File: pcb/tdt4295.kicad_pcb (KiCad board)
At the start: 6 copper layers, 119.8 x 96.8 mm, 156 parts, among them J1 FPGA_DEBUG, J2 DE15_Socket_HighDensity, J4 Conn_ST_STDC14, J5 Micro_SD_Card, J6 Conn_02x05_Odd_Even, J7 USB_C_Receptacle_USB2.0_14P, J8 USB_C_Receptacle_USB2.0_14P, SW1 SW_BLUE, SW2 SW_BLACK, U1 XC7A50T-FTG256, U2 S70KL1283DPBHV020, U3 W25Q128JVS, U4 TPS54325PWP.d, U5 TPS54294PWP, U6 STM32U595ZJTx, U7 TPS2051CDBV, U8 USBLC6-2SC6, Y1 ASE-20MHz, Y2 16MHz

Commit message: fixed psd footprintgs and some routing
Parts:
- J6: footprint Connector_PinHeader_2.54mm:PinHeader_2x05_P2.54mm_Vertical_SMD -> Connector_PinHeader_2.54mm:PinHeader_2x05_P2.54mm_Vertical
- U5: footprint Package_SO:HTSSOP-16-1EP_4.4x5mm_P0.65mm_EP3.4x5mm_Mask2.46x2.31mm -> TPS54294PWP:PWP16_2P31X2P46
- moved J6 5.63 mm to (69.9, 135.3), turned to 90 degrees
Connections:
- J6 pad 1: /Powersupply/5V_IN -> 5V_IN
- J7 pad A4: /power_source/5V_IN -> 5V_IN
- J7 pad A9: /power_source/5V_IN -> 5V_IN
- J7 pad B4: /power_source/5V_IN -> 5V_IN
- J7 pad B9: /power_source/5V_IN -> 5V_IN
- R57 pad 1: /power_source/5V_IN -> 5V_IN
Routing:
- net 5V_IN: track 0.00 -> 29.1 mm, vias 0 -> 2
- net POWER_IN: track 105.4 -> 85.4 mm, vias 6 -> 4
- net USER_BUTTON: track 85.1 -> 76.2 mm
- net GND: track 454.5 -> 459.3 mm, vias 125 -> 123

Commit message: fixed many errors and violations
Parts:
- moved C25 0.24 mm to (123.2, 103.3)
- moved R46 0.11 mm to (134.7, 73.6)
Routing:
- net /Powersupply/1V0_OUT: track 0.00 -> 68.1 mm, vias 0 -> 4
- net /Powersupply/1V8_OUT: track 0.00 -> 48.7 mm, vias 0 -> 2
- net +1V8: track 70.1 -> 111.6 mm, vias 6 -> 11
- net +3V3: track 174.9 -> 213.3 mm, vias 66 -> 68
- net /Powersupply/3V3_OUT: track 11.1 -> 49.1 mm, vias 1 -> 3
- net +1V0: track 114.0 -> 144.5 mm, vias 8 -> 13
- net POWER_IN: track 85.4 -> 95.5 mm
- net GND: track 459.3 -> 469.2 mm, vias 123 -> 122
- net Net-(J8-D+-PadA6): track 7.98 -> 9.72 mm
- net Net-(U7-OUT): track 27.2 -> 28.8 mm
- net Net-(U1A-IO_L23N_T3_A02_D18_14): track 17.2 -> 17.8 mm, vias 1 -> 2

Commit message: fixed all unconnected errors
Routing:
- net +1V8: track 111.6 -> 136.5 mm
- net +1V0: track 144.5 -> 163.4 mm
- net GND: track 469.2 -> 475.9 mm

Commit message: labeled usb data +/- conn and diff-paired them
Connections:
- net Net-(J8-D+-PadA6) renamed /MCU/host_port/D+
- net Net-(J8-D--PadA7) renamed /MCU/host_port/D-
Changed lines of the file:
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@@
 			(layers "F.Cu" "F.Mask" "F.Paste")
 			(roundrect_rratio 0.25)
-			(net "Net-(J8-D+-PadA6)")
+			(net "/MCU/host_port/D+")
 			(pinfunction "I/O1_1")
 			(pintype "passive")
@@
 			(layers "F.Cu" "F.Mask" "F.Paste")
 			(roundrect_rratio 0.25)
-			(net "Net-(J8-D--PadA7)")
+			(net "/MCU/host_port/D-")
 			(pinfunction "I/O2_3")
 			(pintype "passive")
@@
 			(layers "F.Cu" "F.Mask" "F.Paste")
 			(roundrect_rratio 0.25)
-			(net "Net-(J8-D+-PadA6)")
+			(net "/MCU/host_port/D+")
 			(pinfunction "D+_A6")
 			(pintype "bidirectional")
@@
 			(layers "F.Cu" "F.Mask" "F.Paste")
 			(roundrect_rratio 0.25)
-			(net "Net-(J8-D--PadA7)")
+			(net "/MCU/host_port/D-")
 			(pinfunction "D-_A7")
 			(pintype "bidirectional")
@@
 			(layers "F.Cu" "F.Mask" "F.Paste")
 			(roundrect_rratio 0.25)
-			(net "Net-(J8-D+-PadA6)")
+			(net "/MCU/host_port/D+")
 			(pinfunction "D+_B6")
 			(pintype "bidirectional")
@@
 			(layers "F.Cu" "F.Mask" "F.Paste")
 			(roundrect_rratio 0.25)
-			(net "Net-(J8-D--PadA7)")
+			(net "/MCU/host_port/D-")
 			(pinfunction "D-_B7")
 			(pintype "bidirectional")
@@
 	)
 	(segment
-		(start 59.68 89.25)
-		(end 59.178656 89.25)
-		(width 0.15)
-		(layer "F.Cu")
-		(net "Net-(J8-D+-PadA6)")
-	)
-	(segment
-		(start 58.8 89.2)
-		(end 58.85 89.25)
-		(width 0.15)
-		(layer "F.Cu")
-		(net "Net-(J8-D+-PadA6)")
-	)
-	(segment
-		(start 58.65 90.25)
-		(end 58.6 90.2)
-		(width 0.15)
-		(layer "F.Cu")
-		(net "Net-(J8-D+-PadA6)")
-	)
-	(segment
-		(start 58.85 89.25)
-		(end 59.555 89.25)
-		(width 0.15)
-		(layer "F.Cu")
-		(net "Net-(J8-D+-PadA6)")
-	)
-	(segment
-		(start 59.105001 90.25)
-		(end 59.68 90.25)
-		(width 0.15)
-		(layer "F.Cu")
-		(net "Net-(J8-D+-PadA6)")
-	)
-	(segment
-		(start 58.6 90.2)
-		(end 58.6 89.2)
-		(width 0.15)
-		(layer "F.Cu")
-		(net "Net-(J8-D+-PadA6)")
-	)
-	(segment
-		(start 62.825 90)
-		(end 61 90)
-		(width 0.15)
-		(layer "F.Cu")
-		(net "Net-(J8-D+-PadA6)")
-	)
-	(segment
-		(start 64.55 88.275)
-		(end 62.825 90)
-		(width 0.15)
-		(layer "F.Cu")
-		(net "Net-(J8-D+-PadA6)")
-	)
-	(segment
-		(start 58.6 89.2)
-		(end 58.8 89.2)
-		(width 0.15)
-		(layer "F.Cu")
-		(net "Net-(J8-D+-PadA6)")
-	)
-	(segment
-		(start 59.68 90.25)
-		(end 60.75 90.25)
-		(width 0.15)
-		(layer "F.Cu")
-		(net "Net-(J8-D+-PadA6)")
-	)
-	(segment
-		(start 59.555 90.25)
-		(end 58.65 90.25)
-		(width 0.15)
-		(layer "F.Cu")
-		(net "Net-(J8-D+-PadA6)")
-	)
-	(segment
-		(start 60.75 90.25)
-		(end 61 90)
-		(width 0.15)
-		(layer "F.Cu")
-		(net "Net-(J8-D+-PadA6)")
-	)
-	(segment
-		(start 62.1125 87.3875)
-		(end 61 88.5)
-		(width 0.15)
-		(layer "F.Cu")
-		(net "Net-(J8-D--PadA7)")
-	)
-	(segment
-		(start 60.75 88.75)
-		(end 61 88.5)
-		(width 0.15)
-		(layer "F.Cu")
-		(net "Net-(J8-D--PadA7)")
-	)
-	(segment
-		(start 59.68 88.75)
-		(end 60.75 88.75)
-		(width 0.15)
-		(layer "F.Cu")
-		(net "Net-(J8-D--PadA7)")
-	)
-	(segment
-		(start 60.48 89.524999)
-		(end 60.254999 89.75)
-		(width 0.15)
-		(layer "F.Cu")
-		(net "Net-(J8-D--PadA7)")
-	)
-	(segment
-		(start 66.45 88.275)
-		(end 66.45 88.028014)
-		(width 0.15)
-		(layer "F.Cu")
-		(net "Net-(J8-D--PadA7)")
-	)
-	(segment
-		(start 60.48 88.975001)
-		(end 60.48 89.524999)
-		(width 0.15)
-		(layer "F.Cu")
-		(net "Net-(J8-D--PadA7)")
-	)
-	(segment
-		(start 60.254999 89.75)
-		(end 59.68 89.75)
-		(width 0.15)
-		(layer "F.Cu")
-		(net "Net-(J8-D--PadA7)")
-	)
-	(segment
-		(start 65.809486 87.3875)
-		(end 62.1125 87.3875)
-		(width 0.15)
-		(layer "F.Cu")
-		(net "Net-(J8-D--PadA7)")
-	)
-	(segment
-		(start 66.45 88.028014)
-		(end 65.809486 87.3875)
-		(width 0.15)
-		(layer "F.Cu")
-		(net "Net-(J8-D--PadA7)")
-	)
-	(segment
-		(start 59.68 88.75)
-		(end 60.254999 88.75)
-		(width 0.15)
-		(layer "F.Cu")
-		(net "Net-(J8-D--PadA7)")
-	)
-	(segment
-		(start 60.254999 88.75)
-		(end 60.48 88.975001)
-		(width 0.15)
-		(layer "F.Cu")
-		(net "Net-(J8-D--PadA7)")
-	)
-	(segment
 		(start 103.504962 66.749999)
 		(end 104.5 66.749999)
@@
 		(net "5V_IN")
 	)
+	(segment
+		(start 59.68 89.25)
+		(end 59.178656 89.25)
+		(width 0.15)
+		(layer "F.Cu")
+		(net "/MCU/host_port/D+")
+	)
+	(segment
+		(start 58.8 89.2)
+		(end 58.85 89.25)
+		(width 0.15)
+		(layer "F.Cu")
+		(net "/MCU/host_port/D+")
+	)
+	(segment
+		(start 58.65 90.25)
+		(end 58.6 90.2)
+		(width 0.15)
+		(layer "F.Cu")
+		(net "/MCU/host_port/D+")
+	)
+	(segment
+		(start 58.85 89.25)
+		(end 59.555 89.25)
+		(width 0.15)
+		(layer "F.Cu")
+		(net "/MCU/host_port/D+")
+	)
+	(segment
+		(start 62.725 88.275)
+		(end 64.55 88.275)
+		(width 0.15)
+		(layer "F.Cu")
+		(net "/MCU/host_port/D+")
+	)
+	(segment
+		(start 58.6 90.2)
+		(end 58.6 89.2)
+		(width 0.15)
+		(layer "F.Cu")
+		(net "/MCU/host_port/D+")
+	)
+	(segment
+		(start 59.105001 90.25)
+		(end 60.75 90.25)
+		(width 0.15)
+		(layer "F.Cu")
+		(net "/MCU/host_port/D+")
+	)
+	(segment
+		(start 58.6 89.2)
+		(end 58.8 89.2)
+		(width 0.15)
+		(layer "F.Cu")
+		(net "/MCU/host_port/D+")
+	)
+	(segment
+		(start 59.555 90.25)
+		(end 58.65 90.25)
+		(width 0.15)
+		(layer "F.Cu")
+		(net "/MCU/host_port/D+")
+	)
+	(segment
+		(start 60.75 90.25)
+		(end 62.725 88.275)
+		(width 0.15)
+		(layer "F.Cu")
+		(net "/MCU/host_port/D+")
+	)
+	(segment
+		(start 64.025 87.603014)
+		(end 64.240514 87.3875)
+		(width 0.15)
+		(layer "F.Cu")
+		(net "/MCU/host_port/D-")
+	)
+	(segment
+		(start 60.75 88.75)
+		(end 61.625 87.875)
+		(width 0.15)
+		(layer "F.Cu")
+		(net "/MCU/host_port/D-")
+	)
+	(segment
+		(start 64.025 87.875)
+		(end 64.025 87.603014)
+		(width 0.15)
+		(layer "F.Cu")
+		(net "/MCU/host_port/D-")
+	)
+	(segment
+		(start 60.254999 89.75)
+		(end 60.48 89.524999)
+		(width 0.15)
+		(layer "F.Cu")
+		(net "/MCU/host_port/D-")
+	)
+	(segment
+		(start 65.809486 87.3875)
+		(end 66.05 87.628014)
+		(width 0.15)
+		(layer "F.Cu")
+		(net "/MCU/host_port/D-")
+	)
+	(segment
+		(start 66.45 88.275)
+		(end 66.45 88.028014)
+		(width 0.15)
+		(layer "F.Cu")
+		(net "/MCU/host_port/D-")
+	)
+	(segment
+		(start 59.68 89.75)
+		(end 60.254999 89.75)
+		(width 0.15)
+		(layer "F.Cu")
+		(net "/MCU/host_port/D-")
+	)
+	(segment
+		(start 66.05 87.628014)
+		(end 66.05 87.875)
+		(width 0.15)
+		(layer "F.Cu")
+		(net "/MCU/host_port/D-")
+	)
+	(segment
+		(start 60.48 88.975001)
+		(end 60.254999 88.75)
+		(width 0.15)
+		(layer "F.Cu")
+		(net "/MCU/host_port/D-")
+	)
+	(segment
+		(start 64.240514 87.3875)
+		(end 65.809486 87.3875)
+		(width 0.15)
+		(layer "F.Cu")
+		(net "/MCU/host_port/D-")
+	)
+	(segment
+		(start 59.68 88.75)
+		(end 60.75 88.75)
+		(width 0.15)
+		(layer "F.Cu")
+		(net "/MCU/host_port/D-")
+	)
+	(segment
+		(start 61.625 87.875)
+		(end 64.025 87.875)
+		(width 0.15)
+		(layer "F.Cu")
+		(net "/MCU/host_port/D-")
+	)
+	(segment
+		(start 60.254999 88.75)
+		(end 59.68 88.75)
+		(width 0.15)
+		(layer "F.Cu")
+		(net "/MCU/host_port/D-")
+	)
+	(segment
+		(start 60.48 89.524999)
+		(end 60.48 88.975001)
+		(width 0.15)
+		(layer "F.Cu")
+		(net "/MCU/host_port/D-")
+	)
+	(segment
+		(start 66.05 87.875)
+		(end 66.45 88.275)
+		(width 0.15)
+		(layer "F.Cu")
+		(net "/MCU/host_port/D-")
+	)
 	(zone

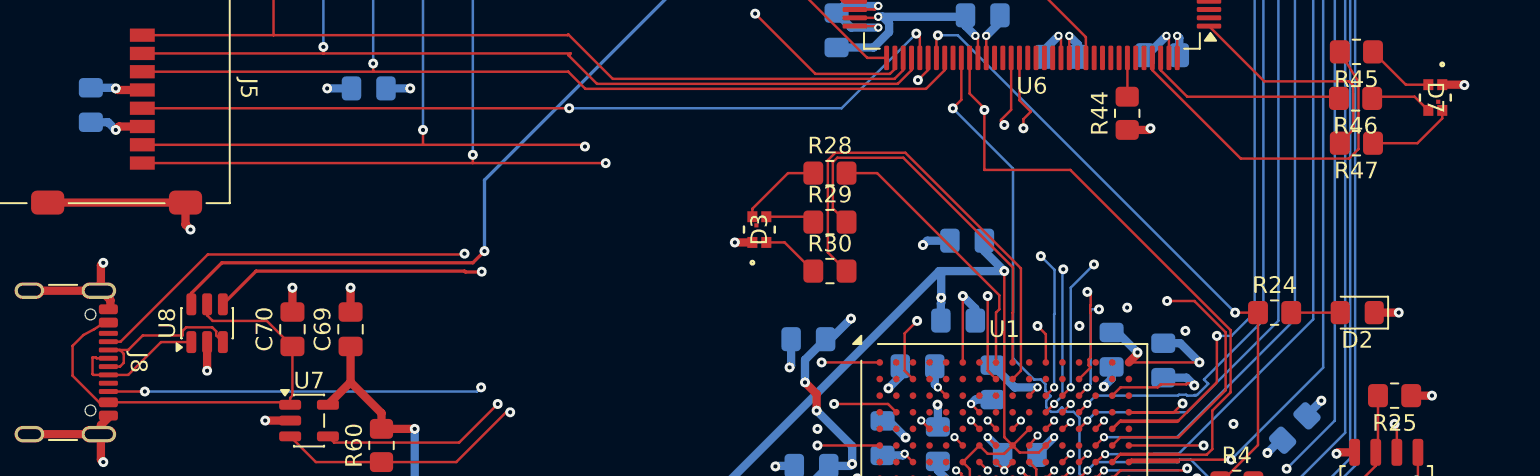
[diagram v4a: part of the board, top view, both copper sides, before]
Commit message: fixed led footprint and model
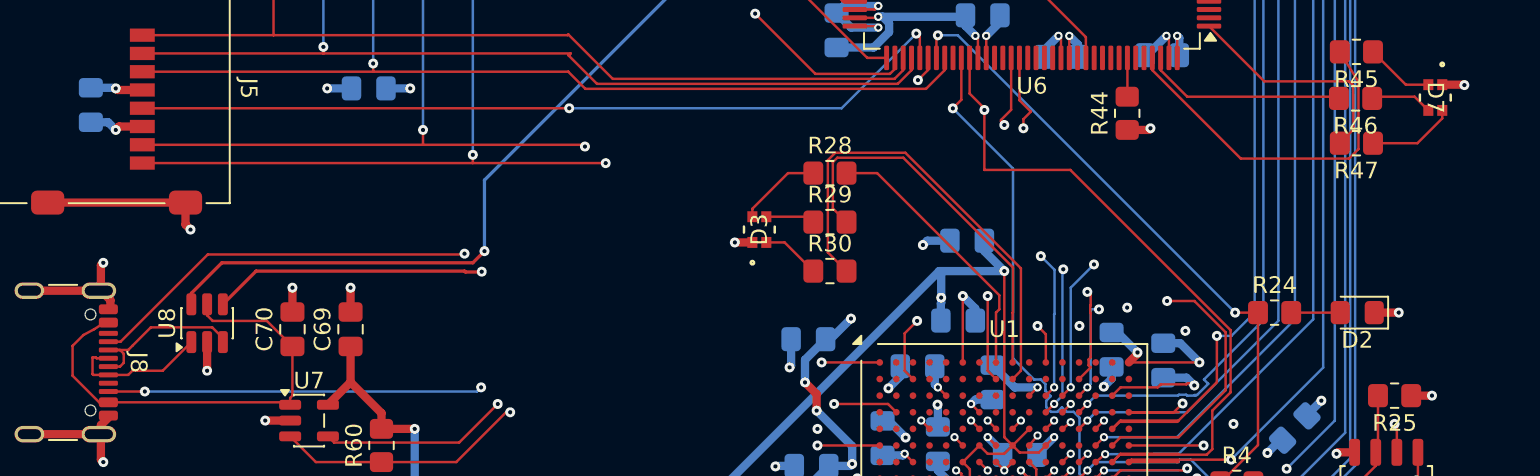
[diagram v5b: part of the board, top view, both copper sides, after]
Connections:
- net /MCU/host_port/D+ renamed Net-(J8-D+-PadA6)
- net /MCU/host_port/D- renamed Net-(J8-D--PadA7)

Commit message: fixed all unconnected wires warnings
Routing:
- net GND: track 475.9 -> 468.0 mm
- net /fpga/TMS_0: track 63.4 -> 55.6 mm
- net P2_IO7: track 34.5 -> 26.8 mm
- net P2_IO6: track 38.0 -> 31.3 mm
- net /fpga/TCK_0: track 61.2 -> 54.5 mm
- net P1_IO4: track 36.9 -> 32.4 mm
- net P1_IO5: track 43.9 -> 40.4 mm, vias 1 -> 0
- net +1V8: track 136.5 -> 133.4 mm, vias 11 -> 8
- net SPI1_MOSI: track 52.6 -> 49.6 mm
- net P2_IO1: track 48.3 -> 45.3 mm
- net FPGA_PROGRAM_B: track 75.0 -> 73.8 mm
- net /fpga/HSYNC: track 123.6 -> 122.7 mm
- net Net-(U1A-IO_L2P_T0_D02_14): track 22.6 -> 21.8 mm
- net Net-(U1C-M0_0): track 22.1 -> 21.4 mm, vias 3 -> 2
- net /fpga/GREEN_ANALOG: vias 3 -> 2
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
